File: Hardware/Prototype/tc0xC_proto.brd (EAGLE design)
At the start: 101.6 x 98.8 mm, 96 parts, among them IC1 AP2112M-3.3TRG1, Q1 2.5A/30V, Q2 MBT3904DW1T1, Q3 600mA/40V, Q4 MBT3904DW1T1, U2 ESP3212, U4 FT231XS, U5 W25Q32FVSS, Y1 26MHz, Y2 32.768kHz

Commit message: cleaned ripped up prototype
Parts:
- added C6: 4.7uF, SparkFun-Capacitors:0603
- added R20: 100, SparkFun-Resistors:0603
- moved D26 88.9 mm to (8.94, 34.5)
- moved C30 83.7 mm to (12.5, 24.5), turned to 270 degrees
- moved C8 77.5 mm to (34.2, 14.5), turned to 270 degrees
- moved C9 77.3 mm to (42.4, 20.8), turned to 180 degrees
- moved C22 73.9 mm to (39.9, 16.9), turned to 90 degrees
- moved R14 69.6 mm to (11.6, 63.7)
- moved R13 68.6 mm to (11.7, 66.0)
- moved C24 66.3 mm to (45.2, 13.2), turned to 90 degrees
- moved R5 62.6 mm to (85.2, 39.3), turned to 90 degrees
- moved C26 62.2 mm to (42.4, 22.4), turned to 180 degrees
- moved R15 60.0 mm to (7.99, 31.6)
- moved C27 58.6 mm to (30.4, 41.4), turned to 180 degrees
- moved R18 58.4 mm to (14.2, 46.3), turned to 180 degrees
- moved C2 58.2 mm to (43.1, 16.9), turned to 90 degrees
- moved C23 54.7 mm to (31.7, 30.8)
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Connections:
- removed net VS: D33.3
- net 3.3V: now also C6.1, D33.3, R20.1, R20.2
- net ACC_INT: now also D33.4
- net GND: now also C6.2

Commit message: matrixed LEDs
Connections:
- new net N$21: D13.P$1, D14.P$1, D15.P$1, D16.P$1
- new net N$22: D17.P$1, D18.P$1, D19.P$1, D20.P$1
- new net N$6: D21.P$1, D22.P$1, D23.P$1, D24.P$1
- net CA1: now also D1.P$2, D13.P$2, D17.P$2, D2.P$1, D21.P$2, D3.P$1, D4.P$1, D5.P$2, D9.P$2
- net CA2: now also D1.P$1, D10.P$2, D14.P$2, D18.P$2, D2.P$2, D22.P$2, D6.P$2, D7.P$1, D8.P$1
- net CA3: now also D11.P$2, D12.P$1, D15.P$2, D19.P$2, D23.P$2, D3.P$2, D5.P$1, D6.P$1, D7.P$2
- net CA4: now also D10.P$1, D11.P$1, D12.P$2, D16.P$2, D20.P$2, D24.P$2, D4.P$2, D8.P$2, D9.P$1
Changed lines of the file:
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@@
 <signal name="CA1">
 <contactref element="U1" pad="21"/>
+<contactref element="D21" pad="P$2"/>
+<contactref element="D1" pad="P$2"/>
+<contactref element="D5" pad="P$2"/>
+<contactref element="D9" pad="P$2"/>
+<contactref element="D13" pad="P$2"/>
+<contactref element="D17" pad="P$2"/>
+<contactref element="D2" pad="P$1"/>
+<contactref element="D4" pad="P$1"/>
+<contactref element="D3" pad="P$1"/>
+<wire x1="51.55" y1="83.693" x2="74.082340625" y2="69.38771875" width="0" layer="19" extent="1-1"/>
+<wire x1="29.017659375" y1="69.38771875" x2="51.55" y2="83.693" width="0" layer="19" extent="1-1"/>
+<wire x1="74.082340625" y1="32.21228125" x2="74.082340625" y2="69.38771875" width="0" layer="19" extent="1-1"/>
+<wire x1="51.55" y1="24.257" x2="74.082340625" y2="32.21228125" width="0" layer="19" extent="1-1"/>
+<wire x1="28.87" y1="28.9" x2="51.55" y2="24.257" width="0" layer="19" extent="1-1"/>
+<wire x1="29.017659375" y1="32.21228125" x2="28.87" y2="28.9" width="0" layer="19" extent="1-1"/>
+<wire x1="20.98731875" y1="26.8224" x2="28.87" y2="28.9" width="0" layer="19" extent="1-1"/>
+<wire x1="14.45698125" y1="21.435059375" x2="20.98731875" y2="26.8224" width="0" layer="19" extent="1-1"/>
+<wire x1="7.9241" y1="16.04771875" x2="14.45698125" y2="21.435059375" width="0" layer="19" extent="1-1"/>
 </signal>
 <signal name="CA2">
 <contactref element="U1" pad="22"/>
+<contactref element="D22" pad="P$2"/>
+<contactref element="D2" pad="P$2"/>
+<contactref element="D6" pad="P$2"/>
+<contactref element="D10" pad="P$2"/>
+<contactref element="D14" pad="P$2"/>
+<contactref element="D18" pad="P$2"/>
+<contactref element="D1" pad="P$1"/>
+<contactref element="D7" pad="P$1"/>
+<contactref element="D8" pad="P$1"/>
+<wire x1="51.55" y1="77.343" x2="80.615221875" y2="74.775059375" width="0" layer="19" extent="1-1"/>
+<wire x1="22.48731875" y1="74.775059375" x2="51.55" y2="77.343" width="0" layer="19" extent="1-1"/>
+<wire x1="27.517659375" y1="32.21228125" x2="22.48731875" y2="74.775059375" width="0" layer="19" extent="1-1"/>
+<wire x1="28.07" y1="29.7" x2="27.517659375" y2="32.21228125" width="0" layer="19" extent="1-1"/>
+<wire x1="22.48731875" y1="26.8224" x2="28.07" y2="29.7" width="0" layer="19" extent="1-1"/>
+<wire x1="51.55" y1="17.907" x2="28.07" y2="29.7" width="0" layer="19" extent="1-1"/>
+<wire x1="50.05" y1="11.557" x2="51.55" y2="17.907" width="0" layer="19" extent="1-1"/>
+<wire x1="50.05" y1="5.207" x2="50.05" y2="11.557" width="0" layer="19" extent="1-1"/>
+<wire x1="80.615221875" y1="26.8224" x2="51.55" y2="17.907" width="0" layer="19" extent="1-1"/>
 </signal>
 <signal name="CA3">
 <contactref element="U1" pad="23"/>
+<contactref element="D5" pad="P$1"/>
+<contactref element="D6" pad="P$1"/>
+<contactref element="D23" pad="P$2"/>
+<contactref element="D3" pad="P$2"/>
+<contactref element="D7" pad="P$2"/>
+<contactref element="D11" pad="P$2"/>
+<contactref element="D15" pad="P$2"/>
+<contactref element="D19" pad="P$2"/>
+<contactref element="D12" pad="P$1"/>
+<wire x1="51.55" y1="90.043" x2="87.145559375" y2="80.1624" width="0" layer="19" extent="1-1"/>
+<wire x1="15.95698125" y1="80.1624" x2="51.55" y2="90.043" width="0" layer="19" extent="1-1"/>
+<wire x1="27.67" y1="29.7" x2="15.95698125" y2="80.1624" width="0" layer="19" extent="1-1"/>
+<wire x1="15.95698125" y1="21.435059375" x2="27.67" y2="29.7" width="0" layer="19" extent="1-1"/>
+<wire x1="50.05" y1="24.257" x2="27.67" y2="29.7" width="0" layer="19" extent="1-1"/>
+<wire x1="50.05" y1="17.907" x2="50.05" y2="24.257" width="0" layer="19" extent="1-1"/>
+<wire x1="51.55" y1="11.557" x2="50.05" y2="17.907" width="0" layer="19" extent="1-1"/>
+<wire x1="87.145559375" y1="21.435059375" x2="51.55" y2="11.557" width="0" layer="19" extent="1-1"/>
+<wire x1="92.1759" y1="16.04771875" x2="87.145559375" y2="21.435059375" width="0" layer="19" extent="1-1"/>
 </signal>
 <signal name="CA8">
@@
 <signal name="CA4">
 <contactref element="U1" pad="24"/>
+<contactref element="D9" pad="P$1"/>
+<contactref element="D10" pad="P$1"/>
+<contactref element="D11" pad="P$1"/>
+<contactref element="D24" pad="P$2"/>
+<contactref element="D16" pad="P$2"/>
+<contactref element="D20" pad="P$2"/>
+<contactref element="D12" pad="P$2"/>
+<contactref element="D8" pad="P$2"/>
+<contactref element="D4" pad="P$2"/>
+<wire x1="51.55" y1="96.393" x2="93.6759" y2="85.55228125" width="0" layer="19" extent="1-1"/>
+<wire x1="9.4241" y1="85.55228125" x2="51.55" y2="96.393" width="0" layer="19" extent="1-1"/>
+<wire x1="72.582340625" y1="32.21228125" x2="93.6759" y2="85.55228125" width="0" layer="19" extent="1-1"/>
+<wire x1="79.115221875" y1="26.8224" x2="72.582340625" y2="32.21228125" width="0" layer="19" extent="1-1"/>
+<wire x1="85.645559375" y1="21.435059375" x2="79.115221875" y2="26.8224" width="0" layer="19" extent="1-1"/>
+<wire x1="93.6759" y1="16.04771875" x2="85.645559375" y2="21.435059375" width="0" layer="19" extent="1-1"/>
+<wire x1="51.55" y1="5.207" x2="72.582340625" y2="32.21228125" width="0" layer="19" extent="1-1"/>
+<wire x1="27.27" y1="29.7" x2="51.55" y2="5.207" width="0" layer="19" extent="1-1"/>
+<wire x1="9.4241" y1="16.04771875" x2="27.27" y2="29.7" width="0" layer="19" extent="1-1"/>
 </signal>
 <signal name="CA5">
@@
 <contactref element="U1" pad="27"/>
 </signal>
+<signal name="N$6">
+<contactref element="D21" pad="P$1"/>
+<contactref element="D22" pad="P$1"/>
+<contactref element="D23" pad="P$1"/>
+<contactref element="D24" pad="P$1"/>
+<wire x1="20.98731875" y1="74.775059375" x2="27.517659375" y2="69.38771875" width="0" layer="19" extent="1-1"/>
+<wire x1="14.45698125" y1="80.1624" x2="20.98731875" y2="74.775059375" width="0" layer="19" extent="1-1"/>
+<wire x1="7.9241" y1="85.55228125" x2="14.45698125" y2="80.1624" width="0" layer="19" extent="1-1"/>
+</signal>
+<signal name="N$21">
+<contactref element="D13" pad="P$1"/>
+<contactref element="D14" pad="P$1"/>
+<contactref element="D15" pad="P$1"/>
+<contactref element="D16" pad="P$1"/>
+<wire x1="85.645559375" y1="80.1624" x2="92.1759" y2="85.55228125" width="0" layer="19" extent="1-1"/>
+<wire x1="79.115221875" y1="74.775059375" x2="85.645559375" y2="80.1624" width="0" layer="19" extent="1-1"/>
+<wire x1="72.582340625" y1="69.38771875" x2="79.115221875" y2="74.775059375" width="0" layer="19" extent="1-1"/>
+</signal>
+<signal name="N$22">
+<contactref element="D17" pad="P$1"/>
+<contactref element="D18" pad="P$1"/>
+<contactref element="D19" pad="P$1"/>
+<contactref element="D20" pad="P$1"/>
+<wire x1="50.05" y1="90.043" x2="50.05" y2="96.393" width="0" layer="19" extent="1-1"/>
+<wire x1="50.05" y1="83.693" x2="50.05" y2="90.043" width="0" layer="19" extent="1-1"/>
+<wire x1="50.05" y1="77.343" x2="50.05" y2="83.693" width="0" layer="19" extent="1-1"/>
+</signal>
 </signals>

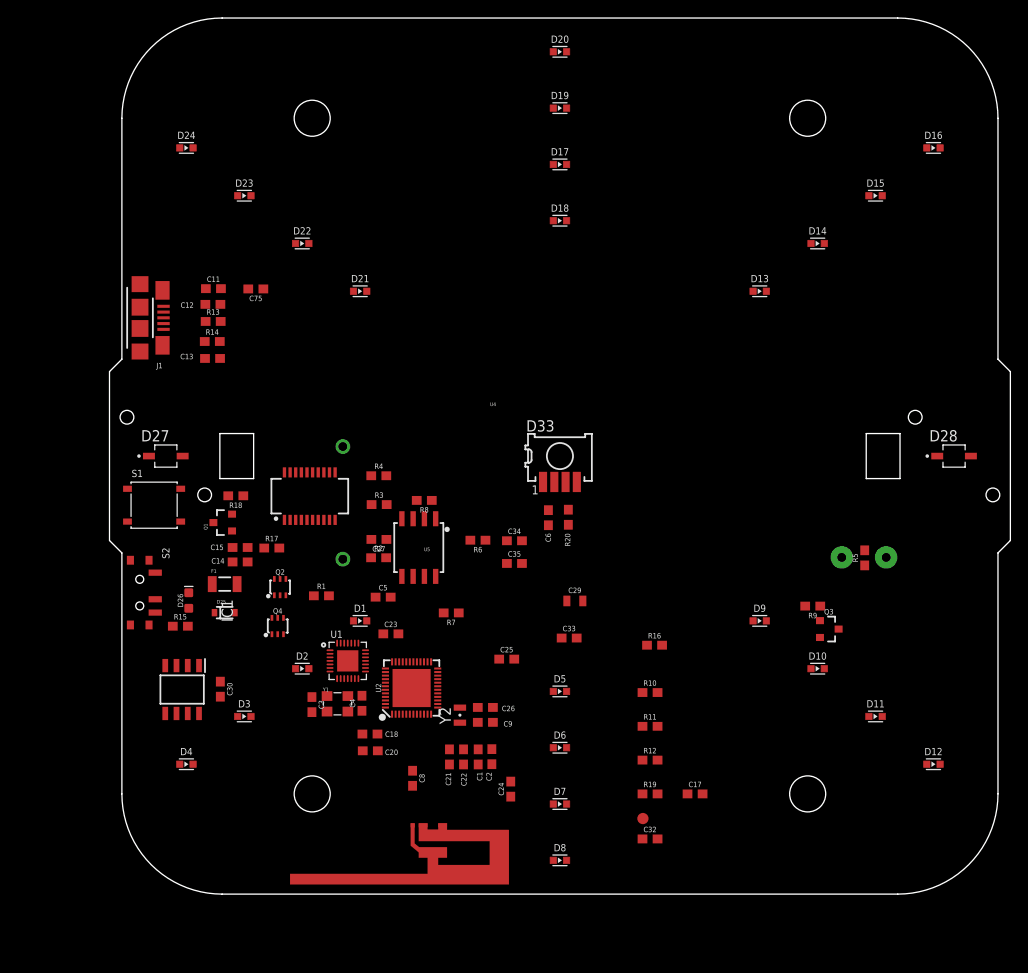
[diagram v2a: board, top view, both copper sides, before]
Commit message: merged tKeepOut and drills
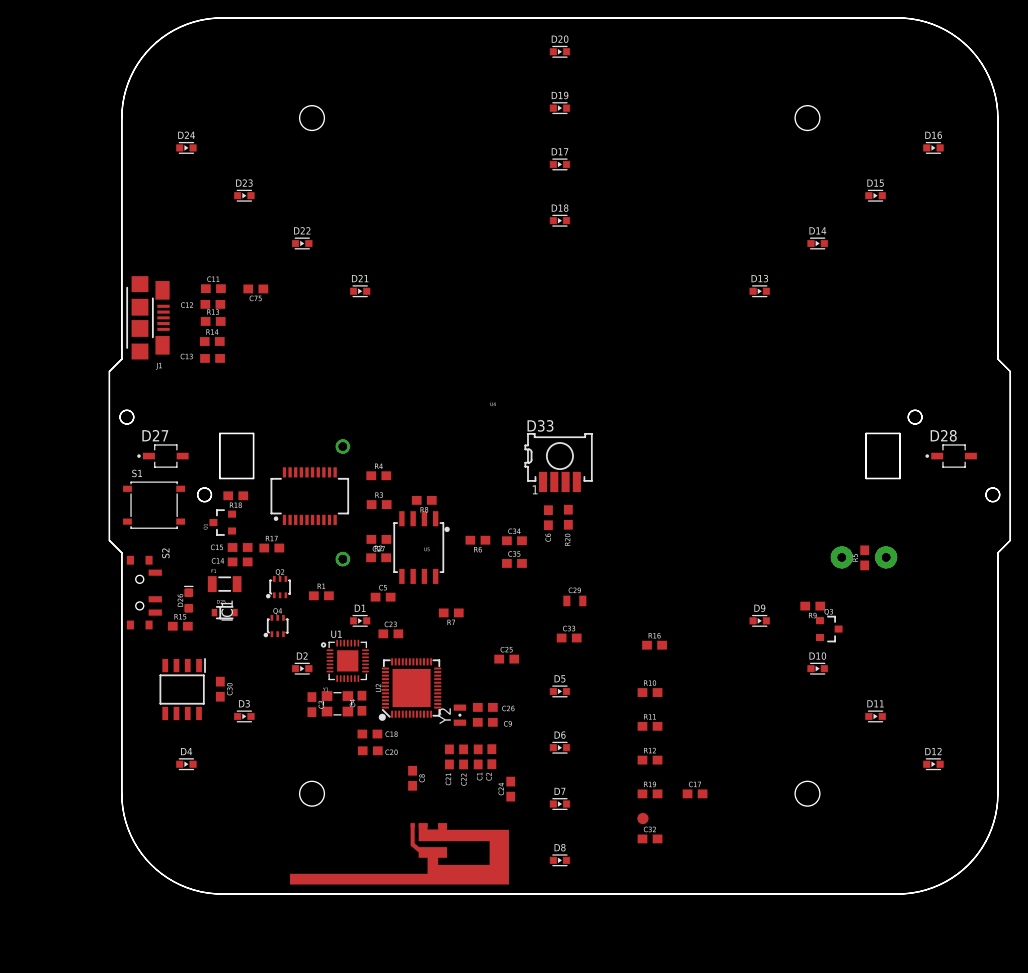
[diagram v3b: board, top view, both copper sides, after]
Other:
- outline, holes or cut-outs redrawn

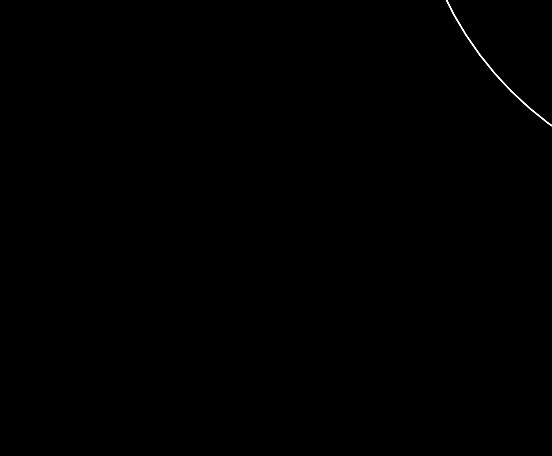
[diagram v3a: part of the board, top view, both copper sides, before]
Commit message: merged tKeepOut and drills
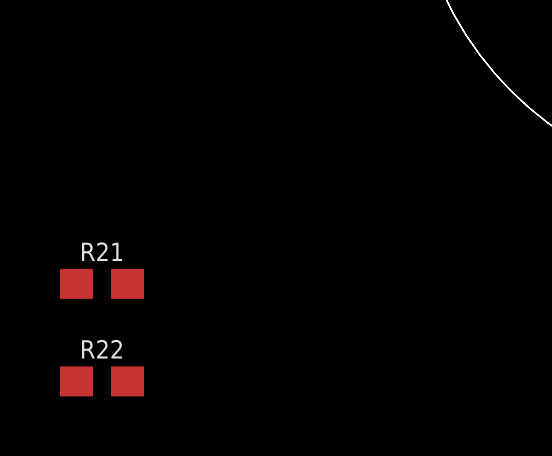
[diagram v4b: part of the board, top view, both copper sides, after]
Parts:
- added R21, R22: 8.2, SparkFun-Resistors:0603
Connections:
- removed net N$21: D13.P$1, D14.P$1, D15.P$1, D16.P$1
- removed net N$22: D17.P$1, D18.P$1, D19.P$1, D20.P$1
- removed net T_START: U2.24
- new net IR_OUT: R21.1, R22.1, U2.24
- new net N$5: D27.A, R21.2
- net CA5: now also D13.P$1, D14.P$1, D15.P$1, D16.P$1
- net CA6: now also D17.P$1, D18.P$1, D19.P$1, D20.P$1
- net CA7: now also D21.P$1, D22.P$1, D23.P$1, D24.P$1
- net GND: now also D27.C, D28.C
- net N$6: now also D28.A, R22.2; no longer D21.P$1, D22.P$1, D23.P$1, D24.P$1
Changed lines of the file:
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@@
 <attribute name="VALUE" x="50.262" y="43.9" size="0.6096" layer="27" font="vector" ratio="20" rot="R90" align="top-center"/>
+</element>
+<element name="R21" library="SparkFun-Resistors" package="0603" value="8.2" x="-8.95" y="-1.7" smashed="yes">
+<attribute name="NAME" x="-8.95" y="-0.938" size="0.6096" layer="25" font="vector" ratio="20" align="bottom-center"/>
+<attribute name="PROD_ID" value="RES-00824" x="-8.95" y="-1.7" size="1.778" layer="27" display="off"/>
+<attribute name="VALUE" x="-8.95" y="-2.462" size="0.6096" layer="27" font="vector" ratio="20" align="top-center"/>
+</element>
+<element name="R22" library="SparkFun-Resistors" package="0603" value="8.2" x="-8.95" y="-4.95" smashed="yes">
+<attribute name="NAME" x="-8.95" y="-4.188" size="0.6096" layer="25" font="vector" ratio="20" align="bottom-center"/>
+<attribute name="PROD_ID" value="RES-00824" x="-8.95" y="-4.95" size="1.778" layer="27" display="off"/>
+<attribute name="VALUE" x="-8.95" y="-5.712" size="0.6096" layer="27" font="vector" ratio="20" align="top-center"/>
 </element>
 </elements>
@@
 <contactref element="D33" pad="1"/>
 <contactref element="C6" pad="2"/>
+<contactref element="D27" pad="C"/>
+<contactref element="D28" pad="C"/>
+<wire x1="80.13" y1="30.34" x2="93.35" y2="50.8" width="0" layer="19" extent="1-1"/>
 <wire x1="66.89" y1="12.7" x2="80.13" y2="30.34" width="0" layer="19" extent="1-1"/>
 <wire x1="60.11" y1="16.51" x2="66.89" y2="12.7" width="0" layer="19" extent="1-1"/>
@@
 <wire x1="26.32" y1="51.87" x2="22.2725" y2="48.9597" width="0" layer="19" extent="1-1"/>
 <wire x1="2.03" y1="47.11" x2="2.36" y2="39.05" width="0" layer="19" extent="1-1"/>
-<wire x1="8.03" y1="47.11" x2="2.03" y2="47.11" width="0" layer="19" extent="1-1"/>
+<wire x1="4.45" y1="50.8" x2="2.03" y2="47.11" width="0" layer="19" extent="1-1"/>
+<wire x1="8.03" y1="47.11" x2="4.45" y2="50.8" width="0" layer="19" extent="1-1"/>
 <wire x1="37.57" y1="9.16" x2="38.34" y2="17.72" width="0" layer="19" extent="1-1"/>
 <wire x1="35.37" y1="9.16" x2="37.57" y2="9.16" width="0" layer="19" extent="1-1"/>
@@
 <wire x1="8.825" y1="21.77" x2="12.5" y2="23.66" width="0" layer="19" extent="1-1"/>
 <wire x1="7.555" y1="21.77" x2="8.825" y2="21.77" width="0" layer="19" extent="1-1"/>
-<wire x1="12.47" y1="61.81" x2="8.03" y2="47.11" width="0" layer="19" extent="1-1"/>
-<wire x1="12.51" y1="67.91" x2="12.47" y2="61.81" width="0" layer="19" extent="1-1"/>
-<wire x1="12.57" y1="69.68" x2="12.51" y2="67.91" width="0" layer="19" extent="1-1"/>
-<wire x1="15.65" y1="69.65" x2="12.57" y2="69.68" width="0" layer="19" extent="1-1"/>
-<wire x1="5.98" y1="69.49" x2="12.57" y2="69.68" width="0" layer="19" extent="1-1"/>
-<wire x1="3.44" y1="70.19" x2="5.98" y2="69.49" width="0" layer="19" extent="1-1"/>
-<wire x1="3.44" y1="67.59" x2="3.44" y2="70.19" width="0" layer="19" extent="1-1"/>
-<wire x1="3.44" y1="65.19" x2="3.44" y2="67.59" width="0" layer="19" extent="1-1"/>
-<wire x1="3.44" y1="62.59" x2="3.44" y2="65.19" width="0" layer="19" extent="1-1"/>
+<wire x1="3.44" y1="62.59" x2="4.45" y2="50.8" width="0" layer="19" extent="1-1"/>
+<wire x1="3.44" y1="65.19" x2="3.44" y2="62.59" width="0" layer="19" extent="1-1"/>
+<wire x1="3.44" y1="67.59" x2="3.44" y2="65.19" width="0" layer="19" extent="1-1"/>
+<wire x1="3.44" y1="70.19" x2="3.44" y2="67.59" width="0" layer="19" extent="1-1"/>
+<wire x1="5.98" y1="69.49" x2="3.44" y2="70.19" width="0" layer="19" extent="1-1"/>
 <wire x1="5.98" y1="63.29" x2="3.44" y2="62.59" width="0" layer="19" extent="1-1"/>
 <wire x1="6.09" y1="65.09" x2="5.98" y2="63.29" width="0" layer="19" extent="1-1"/>
+<wire x1="12.57" y1="69.68" x2="5.98" y2="69.49" width="0" layer="19" extent="1-1"/>
+<wire x1="12.51" y1="67.91" x2="12.57" y2="69.68" width="0" layer="19" extent="1-1"/>
+<wire x1="15.65" y1="69.65" x2="12.57" y2="69.68" width="0" layer="19" extent="1-1"/>
+<wire x1="12.47" y1="61.81" x2="12.51" y2="67.91" width="0" layer="19" extent="1-1"/>
 </signal>
 <signal name="U0RXD">
@@
 <contactref element="U2" pad="21"/>
 </signal>
-<signal name="T_START">
+<signal name="IR_OUT">
 <contactref element="U2" pad="24"/>
+<contactref element="R21" pad="1"/>
+<contactref element="R22" pad="1"/>
+<wire x1="-9.8" y1="-1.7" x2="37.02" y2="26.84" width="0" layer="19" extent="1-1"/>
+<wire x1="-9.8" y1="-4.95" x2="-9.8" y2="-1.7" width="0" layer="19" extent="1-1"/>
 </signal>
 <signal name="BUZZER_OUT">
@@
 <signal name="CA5">
 <contactref element="U1" pad="25"/>
+<contactref element="D16" pad="P$1"/>
+<contactref element="D13" pad="P$1"/>
+<contactref element="D14" pad="P$1"/>
+<contactref element="D15" pad="P$1"/>
+<wire x1="85.645559375" y1="80.1624" x2="92.1759" y2="85.55228125" width="0" layer="19" extent="1-1"/>
+<wire x1="79.115221875" y1="74.775059375" x2="85.645559375" y2="80.1624" width="0" layer="19" extent="1-1"/>
+<wire x1="72.582340625" y1="69.38771875" x2="79.115221875" y2="74.775059375" width="0" layer="19" extent="1-1"/>
+<wire x1="26.87" y1="29.7" x2="72.582340625" y2="69.38771875" width="0" layer="19" extent="1-1"/>
 </signal>
 <signal name="CA6">
 <contactref element="U1" pad="26"/>
+<contactref element="D17" pad="P$1"/>
+<contactref element="D18" pad="P$1"/>
+<contactref element="D19" pad="P$1"/>
+<contactref element="D20" pad="P$1"/>
+<wire x1="50.05" y1="90.043" x2="50.05" y2="96.393" width="0" layer="19" extent="1-1"/>
+<wire x1="50.05" y1="83.693" x2="50.05" y2="90.043" width="0" layer="19" extent="1-1"/>
+<wire x1="50.05" y1="77.343" x2="50.05" y2="83.693" width="0" layer="19" extent="1-1"/>
+<wire x1="26.47" y1="29.7" x2="50.05" y2="77.343" width="0" layer="19" extent="1-1"/>
 </signal>
 <signal name="CA7">
 <contactref element="U1" pad="27"/>
-</signal>
-<signal name="N$6">
 <contactref element="D21" pad="P$1"/>
 <contactref element="D22" pad="P$1"/>
@@
 <wire x1="14.45698125" y1="80.1624" x2="20.98731875" y2="74.775059375" width="0" layer="19" extent="1-1"/>
 <wire x1="7.9241" y1="85.55228125" x2="14.45698125" y2="80.1624" width="0" layer="19" extent="1-1"/>
-</signal>
-<signal name="N$21">
-<contactref element="D13" pad="P$1"/>
-<contactref element="D14" pad="P$1"/>
-<contactref element="D15" pad="P$1"/>
-<contactref element="D16" pad="P$1"/>
-<wire x1="85.645559375" y1="80.1624" x2="92.1759" y2="85.55228125" width="0" layer="19" extent="1-1"/>
-<wire x1="79.115221875" y1="74.775059375" x2="85.645559375" y2="80.1624" width="0" layer="19" extent="1-1"/>
-<wire x1="72.582340625" y1="69.38771875" x2="79.115221875" y2="74.775059375" width="0" layer="19" extent="1-1"/>
-</signal>
-<signal name="N$22">
-<contactref element="D17" pad="P$1"/>
-<contactref element="D18" pad="P$1"/>
-<contactref element="D19" pad="P$1"/>
-<contactref element="D20" pad="P$1"/>
-<wire x1="50.05" y1="90.043" x2="50.05" y2="96.393" width="0" layer="19" extent="1-1"/>
-<wire x1="50.05" y1="83.693" x2="50.05" y2="90.043" width="0" layer="19" extent="1-1"/>
-<wire x1="50.05" y1="77.343" x2="50.05" y2="83.693" width="0" layer="19" extent="1-1"/>
+<wire x1="26.07" y1="29.7" x2="27.517659375" y2="69.38771875" width="0" layer="19" extent="1-1"/>
+</signal>
+<signal name="N$5">
+<contactref element="D27" pad="A"/>
+<contactref element="R21" pad="2"/>
+<wire x1="-8.1" y1="-1.7" x2="8.25" y2="50.8" width="0" layer="19" extent="1-1"/>
+</signal>
+<signal name="N$6">
+<contactref element="D28" pad="A"/>
+<contactref element="R22" pad="2"/>
+<wire x1="-8.1" y1="-4.95" x2="97.15" y2="50.8" width="0" layer="19" extent="1-1"/>
 </signal>
 </signals>
